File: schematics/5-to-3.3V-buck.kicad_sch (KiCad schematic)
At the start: 4 parts, among them U3 TPS62203DBVTG4

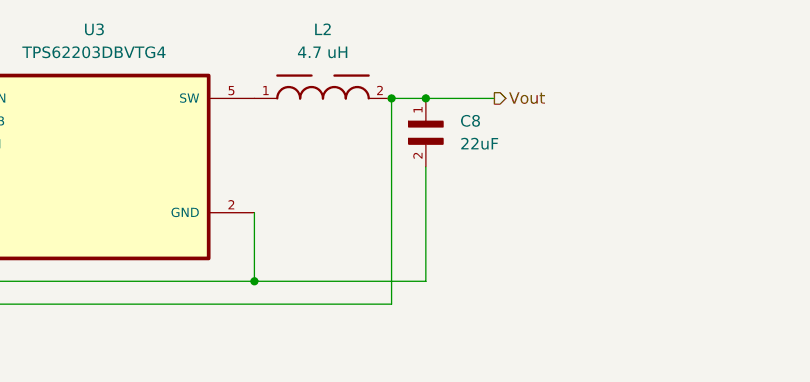
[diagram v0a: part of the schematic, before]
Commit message: Added accelerometer + gyroscope
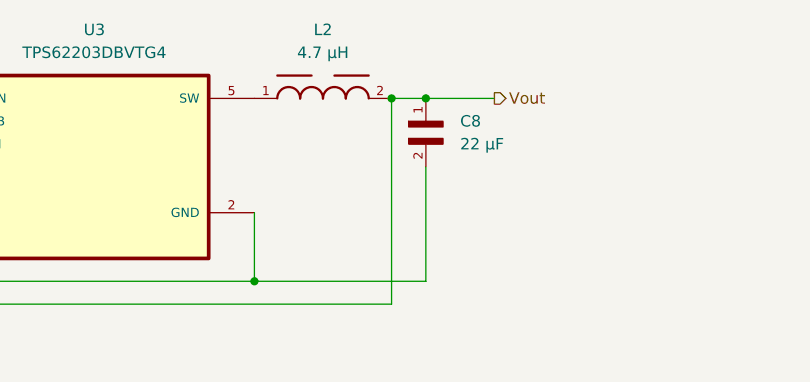
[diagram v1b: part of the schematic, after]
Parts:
- C8: value 22uF -> 22 µF
- L2: value 4.7 uH -> 4.7 µH
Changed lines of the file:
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@@
 			)
 		)
-		(property "Value" "22uF"
+		(property "Value" "22 µF"
 			(at 116.84 29.2099 90)
 			(effects
@@
 			)
 		)
-		(property "Value" "4.7 uH"
+		(property "Value" "4.7 µH"
 			(at 101.6 19.05 0)
 			(effects
